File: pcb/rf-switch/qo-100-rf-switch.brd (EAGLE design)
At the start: 66 x 40 mm, 32 parts, among them U1 F2915NBGK, U2 ADP7142AUJZ-3.3

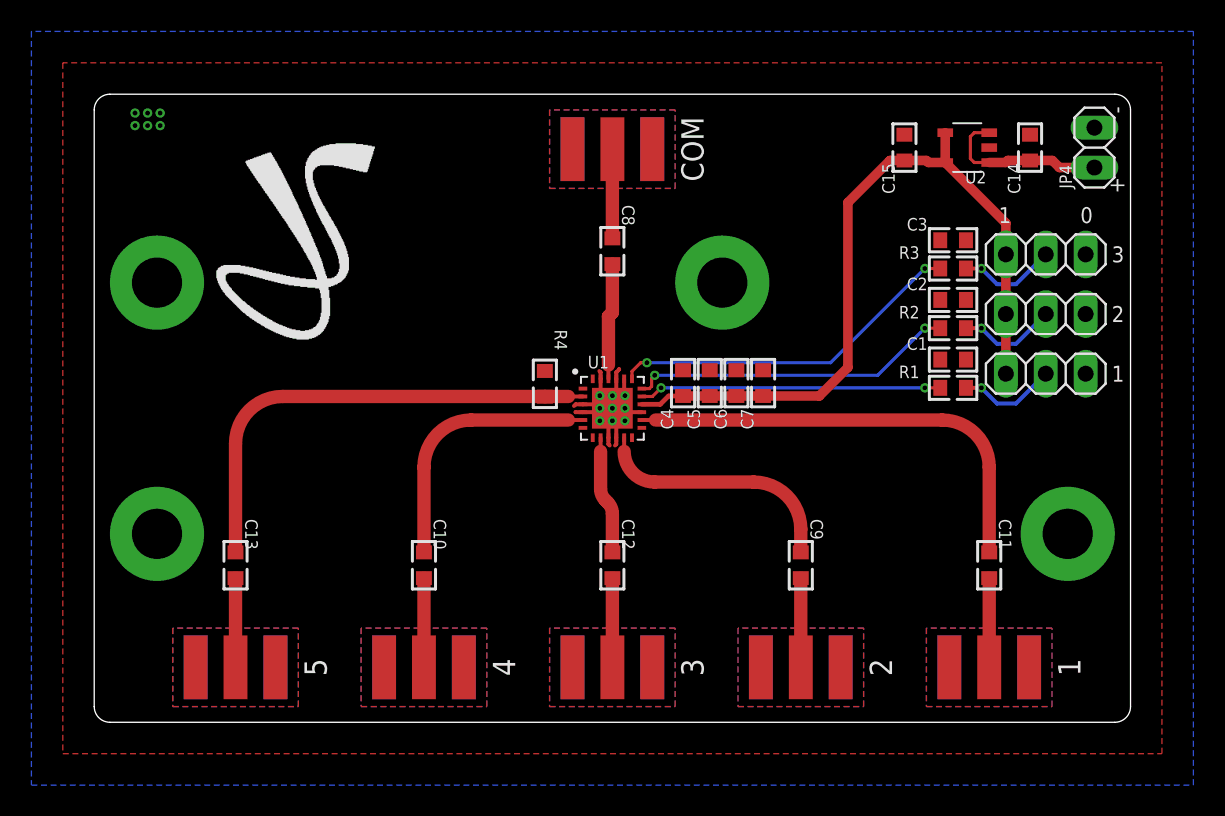
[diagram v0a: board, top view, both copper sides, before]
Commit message: Finished RF switch Added Digital RF power detector Added Orange Pi control hat
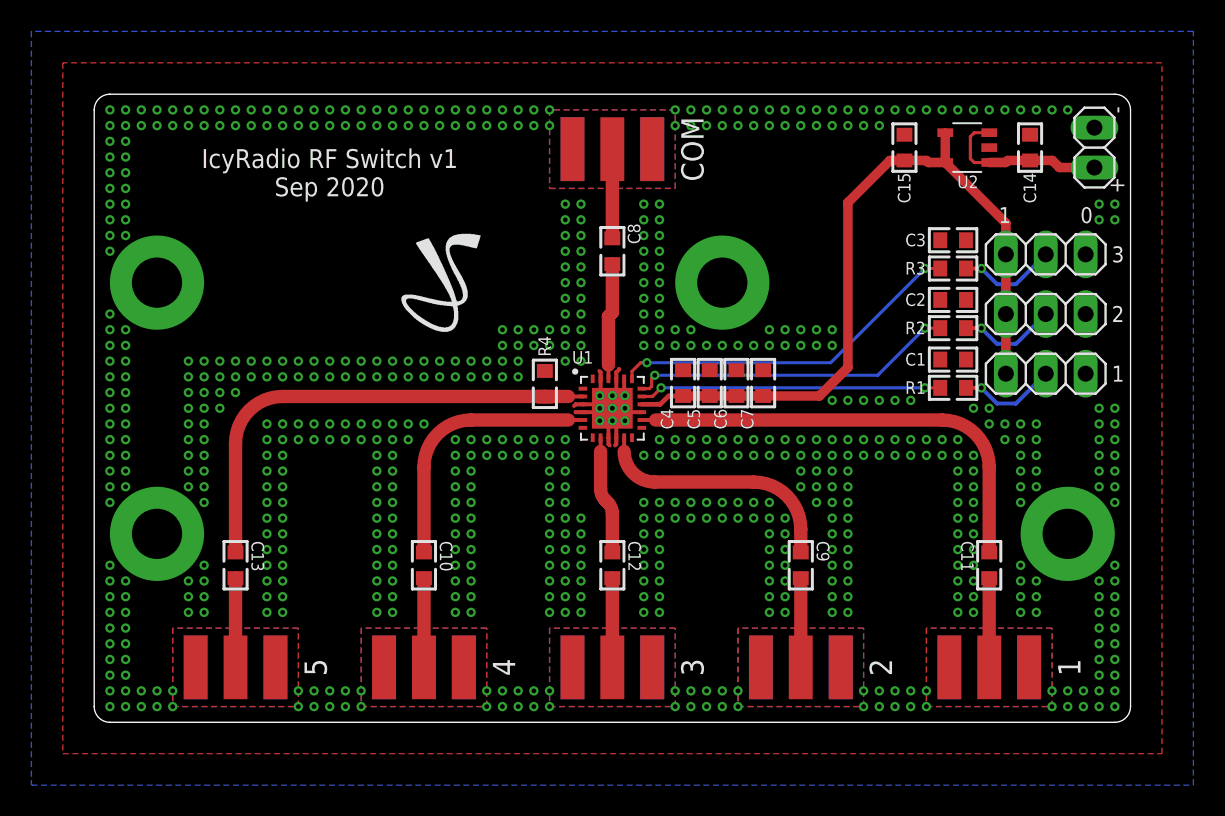
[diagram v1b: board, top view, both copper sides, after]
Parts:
- LOGO1: value JS-10MM -> JS-5MM; device Silkscreen:JS_10MM -> Silkscreen:JS_5MM
- moved LOGO1 8.56 mm to (24.8, 31.3)
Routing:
- net GND: vias 16 -> 681
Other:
- board text added: "IcyRadio RF Switch v1 Sep 2020"

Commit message: Renamed RF Power meter Added Power meter Added IO expander to RF switch PCB to make it work thru I2C
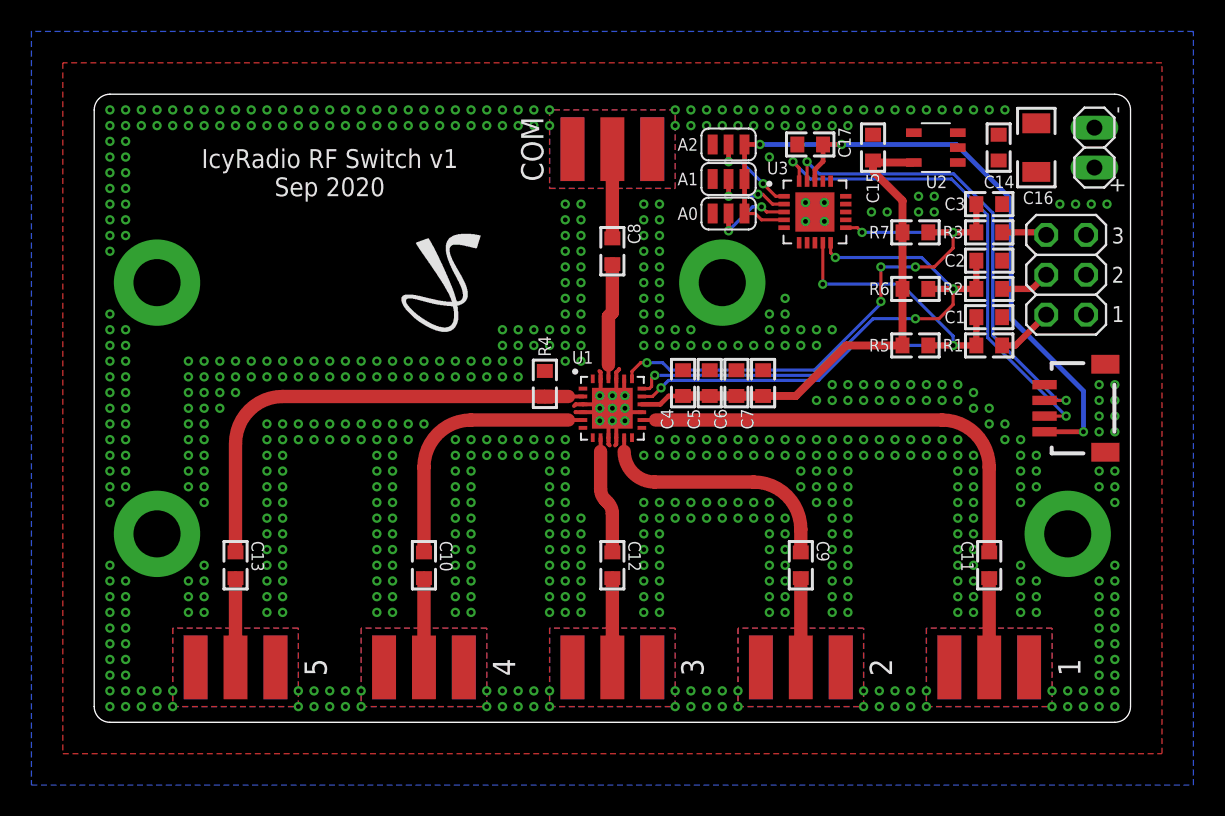
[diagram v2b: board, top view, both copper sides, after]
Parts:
- removed JP2, JP3: PINHD-1X3, Pin Header:1X03
- added C16: 22uF, Capacitor:CAP1206
- added C17: 1uF, Capacitor:CAP0603
- added CON1: 4P-SH-SIDE, JST:SH-04-SIDE
- added R5, R6, R7: 1K Ohms, Resistor:RES0603
- added SJ1, SJ2, SJ3: (no value), Solder Jumper:SJ2_S
- added U3: MCP23008, Microchip:QFN20
- JP1: value PINHD-1X3 -> PINHD-2X3; device Pin Header:1X03 -> Pin Header:2X03
- R1, R2, R3: value 5.1K Ohms -> 1K Ohms
- moved JP1 6.43 mm to (61.9, 28.5), turned to 270 degrees
- moved C1 3.55 mm to (57.0, 25.8)
- moved R1 3.55 mm to (57.0, 24.0)
- moved C2 3.40 mm to (57.0, 29.4)
- moved R2 3.40 mm to (57.0, 27.6)
- moved C3 3.25 mm to (57.0, 33.0)
- moved R3 3.25 mm to (57.0, 31.2)
- moved C14 2.00 mm to (57.6, 36.6)
- moved C15 2.00 mm to (49.6, 36.6)
- moved U2 2.00 mm to (53.6, 36.6)
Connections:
- new net 3V3_IO: C17.1, CON1.1, SJ1.3, SJ2.3, SJ3.3, U3.18, U3.4
- new net I2C_SCL: CON1.3, U3.19
- new net I2C_SDA: CON1.2, U3.20
- new net IO_A0: SJ1.2, U3.3
- new net IO_A1: SJ2.2, U3.2
- new net IO_A2: SJ3.2, U3.1
- net 3V3: now also R5.2, R6.2, R7.2; no longer JP1.1, JP2.1, JP3.1
- net GND: now also C16.2, C17.2, CON1.4, JP1.2, JP1.4, JP1.6, SJ1.1, SJ2.1, SJ3.1, U3.17, U3.PAD; no longer JP1.3, JP2.3, JP3.3
- net N$13: now also JP1.1, R3.2; no longer JP1.2, R1.2
- net N$14: now also JP1.3; no longer JP2.2
- net N$15: now also JP1.5, R1.2; no longer JP3.2, R3.2
- net N$16: now also C16.1
- net SW_V1: now also R5.1, U3.9
- net SW_V2: now also R6.1, U3.10
- net SW_V3: now also R7.1, U3.11
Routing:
- net 3V3_IO: track 0.00 -> 48.4 mm, vias 0 -> 3
- net I2C_SDA: track 0.00 -> 31.5 mm, vias 0 -> 2
- net I2C_SCL: track 0.00 -> 30.0 mm, vias 0 -> 2
- net SW_V1: track 19.2 -> 38.9 mm, vias 2 -> 3
- net SW_V2: track 20.9 -> 37.6 mm, vias 2 -> 4
- net SW_V3: track 22.8 -> 38.8 mm, vias 2 -> 6
- net 3V3: track 48.9 -> 33.4 mm
- net N$16: track 10.9 -> 0.00 mm
- net IO_A2: track 0.00 -> 5.55 mm, vias 0 -> 2
- net IO_A0: track 0.00 -> 5.40 mm, vias 0 -> 2
- net IO_A1: track 0.00 -> 4.95 mm, vias 0 -> 2
- net N$13: track 6.28 -> 2.88 mm, vias 1 -> 0
- net N$14: track 6.28 -> 3.18 mm, vias 1 -> 0
- net N$15: track 6.28 -> 3.62 mm, vias 1 -> 0
- net GND: vias 681 -> 699
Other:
- board text added: "A0"
- board text added: "A1"
- board text added: "A2"
- board text removed: "0"

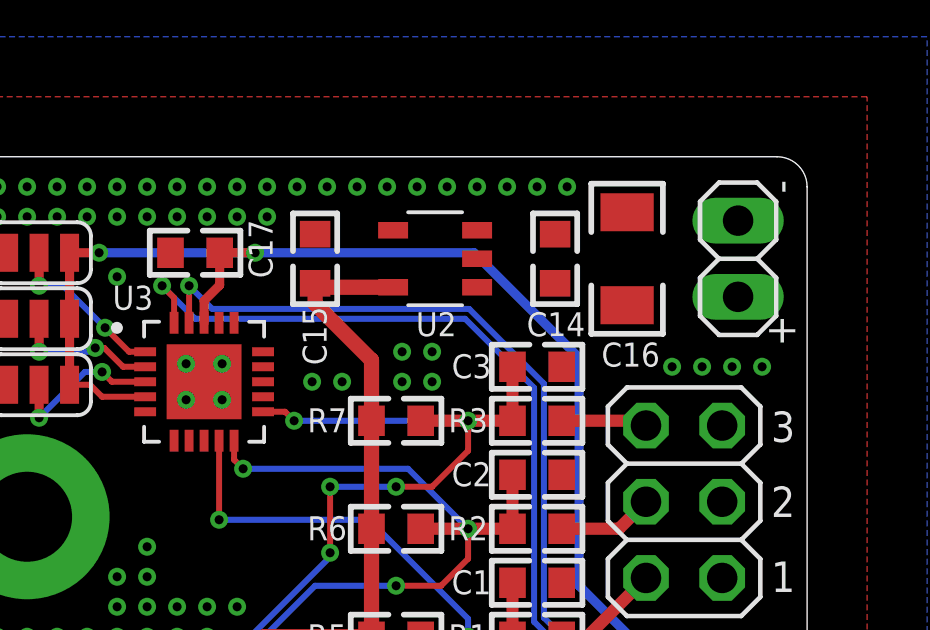
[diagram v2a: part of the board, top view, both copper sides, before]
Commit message: Update libraries on RF switch
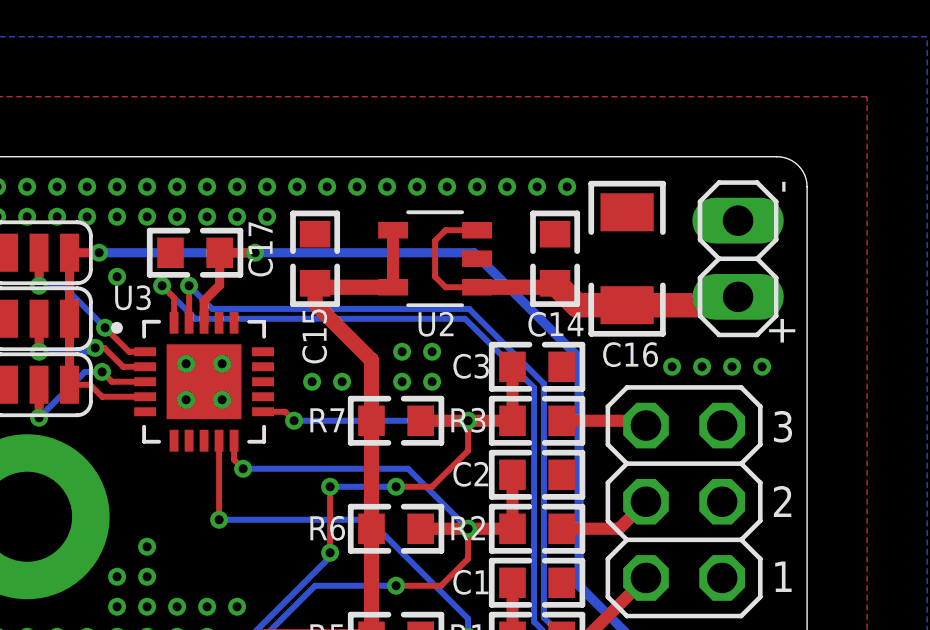
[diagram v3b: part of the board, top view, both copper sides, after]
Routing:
- net N$16: track 0.00 -> 13.5 mm
- net 3V3: track 33.4 -> 35.3 mm
- net GND: track 12.6 -> 13.5 mm
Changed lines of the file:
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@@
 <drawing>
 <settings>
-<setting alwaysvectorfont="yes"/>
+<setting alwaysvectorfont="no"/>
 <setting verticaltext="up"/>
 </settings>
-<grid distance="0.5" unitdist="mm" unit="mm" style="lines" multiple="1" display="yes" altdistance="0.1" altunitdist="mm" altunit="mm"/>
+<grid distance="0.1" unitdist="mm" unit="mm" style="lines" multiple="1" display="yes" altdistance="0.1" altunitdist="mm" altunit="mm"/>
 <layers>
 <layer number="1" name="Top" color="4" fill="1" visible="yes" active="yes"/>
@@
 <via x="46.5" y="31.9" extent="1-16" drill="0.3"/>
 <via x="43" y="36" extent="1-16" drill="0.3"/>
-<wire x1="45.3" y1="31.9" x2="45.9" y2="32.5" width="0" layer="19" extent="1-1"/>
+<wire x1="45.9" y1="32.5" x2="45.3" y2="31.9" width="0.4064" layer="1"/>
 </signal>
 <signal name="SW_V1">
@@
 <wire x1="47.9" y1="24" x2="51.48085" y2="24" width="0.508" layer="1"/>
 <wire x1="44.68085" y1="20.78085" x2="47.9" y2="24" width="0.508" layer="1"/>
-<wire x1="52.2" y1="35.65" x2="52.2" y2="37.55" width="0" layer="19" extent="1-1"/>
+<wire x1="52.2" y1="37.55" x2="52.2" y2="35.65" width="0.4064" layer="1"/>
 </signal>
 <signal name="N$14">
@@
 <contactref element="C14" pad="1"/>
 <contactref element="C16" pad="1"/>
-<wire x1="60" y1="35.0506" x2="63.7" y2="35.33" width="0" layer="19" extent="1-1"/>
-<wire x1="57.6" y1="35.78085" x2="60" y2="35.0506" width="0" layer="19" extent="1-1"/>
-<wire x1="55" y1="35.65" x2="57.6" y2="35.78085" width="0" layer="19" extent="1-1"/>
-<wire x1="55" y1="37.55" x2="55" y2="35.65" width="0" layer="19" extent="1-1"/>
+<wire x1="55" y1="35.65" x2="57.46915" y2="35.65" width="0.508" layer="1"/>
+<wire x1="57.46915" y1="35.65" x2="57.6" y2="35.78085" width="0.508" layer="1"/>
+<wire x1="60" y1="35.0506" x2="58.33025" y2="35.0506" width="0.8128" layer="1"/>
+<wire x1="58.33025" y1="35.0506" x2="57.6" y2="35.78085" width="0.8128" layer="1"/>
+<wire x1="63.7" y1="35.33" x2="63.4206" y2="35.0506" width="0.8128" layer="1"/>
+<wire x1="63.4206" y1="35.0506" x2="60" y2="35.0506" width="0.8128" layer="1"/>
+<wire x1="55" y1="35.65" x2="53.95" y2="35.65" width="0.2" layer="1"/>
+<wire x1="53.95" y1="35.65" x2="53.6" y2="36" width="0.2" layer="1"/>
+<wire x1="53.6" y1="36" x2="53.6" y2="37.2" width="0.2" layer="1"/>
+<wire x1="53.6" y1="37.2" x2="53.95" y2="37.55" width="0.2" layer="1"/>
+<wire x1="53.95" y1="37.55" x2="55" y2="37.55" width="0.2" layer="1"/>
 </signal>
 <signal name="I2C_SDA">
